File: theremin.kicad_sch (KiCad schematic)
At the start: 27 parts, among them J1 Audio Out, J2 12VAC, U2 L7812, U3 L7912

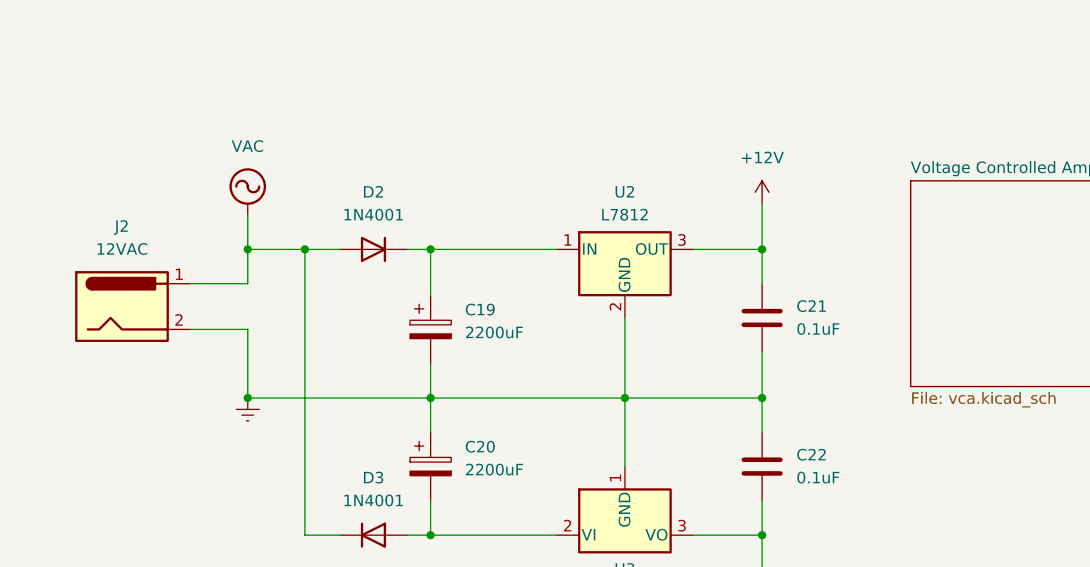
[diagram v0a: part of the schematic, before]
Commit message: Placed in smd and through.
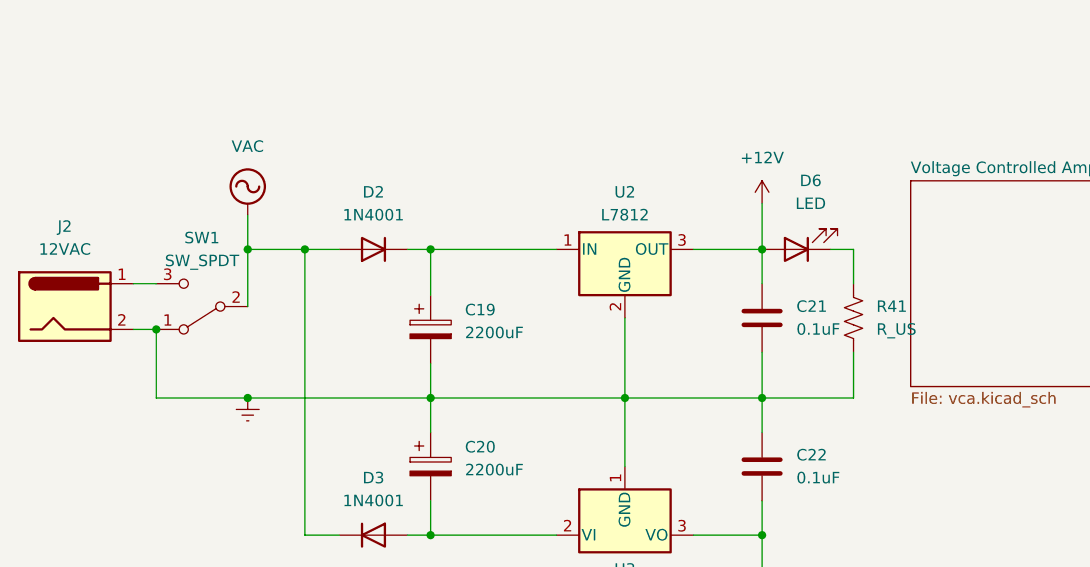
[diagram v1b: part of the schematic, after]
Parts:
- added D6: LED, LED_THT:LED_D3.0mm_Horizontal_O1.27mm_Z2.0mm_IRGrey, symbol Device:LED
- added R41: R_US, Resistor_SMD:R_0805_2012Metric, symbol Device:R_US
- added SW1: SW_SPDT, Button_Switch_THT:SW_SPST_Omron_B3F-315x_Angled, symbol Switch:SW_SPDT
- AE1, AE2: footprint Connector_Coaxial:BNC_Amphenol_031-5539_Vertical -> Connector_Pin:Pin_D1.3mm_L11.0mm
- C12: footprint Capacitor_THT:C_Disc_D11.0mm_W5.0mm_P7.50mm -> Capacitor_SMD:C_0805_2012Metric
- C19, C20: footprint Capacitor_THT:CP_Radial_D10.0mm_P3.80mm -> Capacitor_THT:CP_Radial_D10.0mm_P3.50mm
- C21, C22: footprint Capacitor_THT:C_Disc_D11.0mm_W5.0mm_P7.50mm -> Capacitor_SMD:C_1812_4532Metric
- D1: footprint Diode_THT:D_DO-35_SOD27_P7.62mm_Horizontal -> Diode_SMD:D_2010_5025Metric
- D2, D3: footprint Diode_THT:D_DO-41_SOD81_P10.16mm_Horizontal -> Diode_SMD:D_2010_5025Metric
- L1, L10, L2, L3, L4, L7, L8, L9: footprint Inductor_THT:L_Axial_L7.0mm_D3.3mm_P12.70mm_Horizontal_Fastron_MICC -> Inductor_SMD:L_1210_3225Metric
- R14: footprint Resistor_THT:R_Axial_DIN0207_L6.3mm_D2.5mm_P10.16mm_Horizontal -> Resistor_SMD:R_0805_2012Metric
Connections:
- net +12V: now also D6.2 (A)
- net Earth: now also R41.1, SW1.1 (A)
- net VAC: now also SW1.2 (B); no longer J2.1
- new net: D6.1 (K), R41.2
- new net: J2.1, SW1.3 (C)
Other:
- moved on the sheet: J2

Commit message: Layout cleanup for smd and through
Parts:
- J2: footprint Connector_BarrelJack:BarrelJack_CUI_PJ-063AH_Horizontal_CircularHoles -> Connector_BarrelJack:BarrelJack_CUI_PJ-063AH_Horizontal
- SW1: footprint Button_Switch_THT:SW_SPST_Omron_B3F-315x_Angled -> Button_Switch_THT:SW_Push_1P2T_Vertical_E-Switch_800UDP8P1A1M6
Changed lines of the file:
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@@
       (effects (font (size 1.27 1.27)))
     )
-    (property "Footprint" "Button_Switch_THT:SW_SPST_Omron_B3F-315x_Angled" (at 34.29 140.97 0)
+    (property "Footprint" "Button_Switch_THT:SW_Push_1P2T_Vertical_E-Switch_800UDP8P1A1M6" (at 34.29 140.97 0)
       (effects (font (size 1.27 1.27)) hide)
     )
@@
       (effects (font (size 1.27 1.27)))
     )
-    (property "Footprint" "Connector_BarrelJack:BarrelJack_CUI_PJ-063AH_Horizontal_CircularHoles" (at 20.32 141.986 0)
+    (property "Footprint" "Connector_BarrelJack:BarrelJack_CUI_PJ-063AH_Horizontal" (at 20.32 141.986 0)
       (effects (font (size 1.27 1.27)) hide)
     )
